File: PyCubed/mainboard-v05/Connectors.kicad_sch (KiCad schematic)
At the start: 28 parts, among them J1 503182-1852, J11 35362-0650, J13 USB_C_pycubed, J16 1985807, J18 1985807, J19 35362-0650, J2 Conn_01x05, J20 35362-0650, J21 35362-0650, J22 35362-0650, J23 35362-0650, J3 35362-0650, J4 35362-0650, J8 1985807, J9 1985807, U8 MR25H40MDF

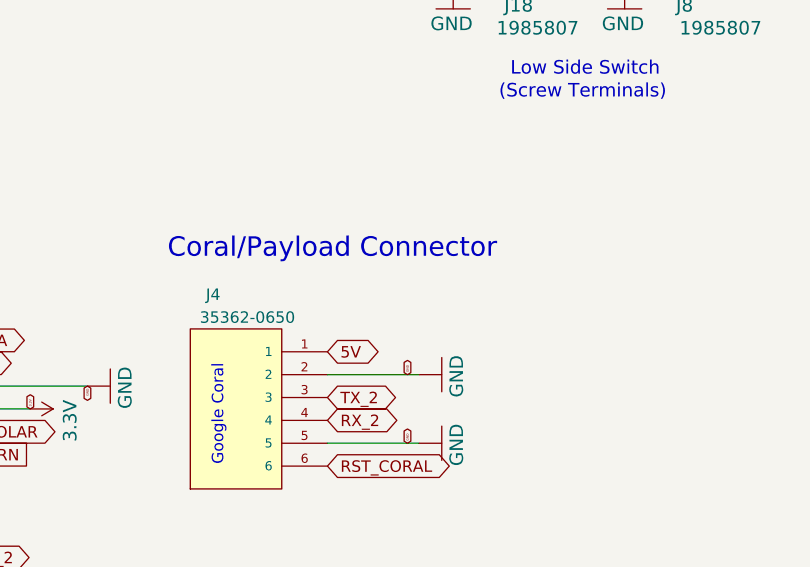
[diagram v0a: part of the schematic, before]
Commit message: final updates after JLC i2c error
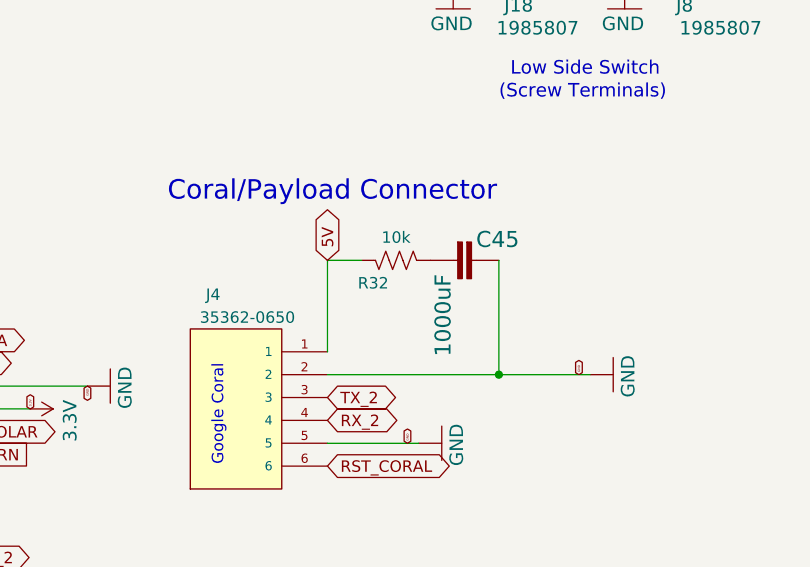
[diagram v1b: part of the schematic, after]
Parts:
- added C45: 1000uF, Capacitor_Tantalum_SMD:CP_EIA-7361-38_AVX-V, symbol mainboard:2.2UF-0603-10V-20%
- added R32: 10k, Resistor_SMD:R_0603_1608Metric, symbol Device:R_US
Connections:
- net 5V: now also R32.2
- net GND: now also C45.1
- new net: C45.2, R32.1
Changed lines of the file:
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@@
   (junction (at 123.19 78.74) (diameter 0) (color 0 0 0 0)
+  )
+  (junction (at 199.39 132.08) (diameter 0) (color 0 0 0 0)
   )
   (junction (at 242.57 41.91) (diameter 0) (color 0 0 0 0)
@@
     (stroke (width 0) (type default) (color 0 0 0 0))
   )
-  (wire (pts (xy 180.34 132.08) (xy 190.5 132.08))
+  (wire (pts (xy 199.39 132.08) (xy 209.55 132.08))
     (stroke (width 0) (type default) (color 0 0 0 0))
   )
@@
     (stroke (width 0) (type default) (color 0 0 0 0))
   )
+  (wire (pts (xy 199.39 119.38) (xy 199.39 132.08))
+    (stroke (width 0) (type default) (color 0 0 0 0))
+  )
   (wire (pts (xy 232.41 50.8) (xy 232.41 49.53))
     (stroke (width 0) (type default) (color 0 0 0 0))
@@
     (stroke (width 0) (type default) (color 0 0 0 0))
   )
+  (wire (pts (xy 180.34 119.38) (xy 184.15 119.38))
+    (stroke (width 0) (type default) (color 0 0 0 0))
+  )
   (wire (pts (xy 148.59 55.88) (xy 151.13 55.88))
     (stroke (width 0) (type default) (color 0 0 0 0))
@@
     (stroke (width 0) (type default) (color 0 0 0 0))
   )
+  (wire (pts (xy 180.34 132.08) (xy 199.39 132.08))
+    (stroke (width 0) (type default) (color 0 0 0 0))
+  )
   (wire (pts (xy 113.03 33.02) (xy 123.19 33.02))
     (stroke (width 0) (type default) (color 0 0 0 0))
@@
   )
   (wire (pts (xy 153.67 181.61) (xy 139.7 181.61))
+    (stroke (width 0) (type default) (color 0 0 0 0))
+  )
+  (wire (pts (xy 180.34 119.38) (xy 180.34 129.54))
     (stroke (width 0) (type default) (color 0 0 0 0))
   )
@@
     (effects (font (size 2.159 2.159)) (justify left bottom))
   )
-  (text "Coral/Payload Connector" (at 162.56 119.38 0)
+  (text "Coral/Payload Connector" (at 162.56 113.03 0)
     (effects (font (size 2.159 2.159)) (justify left bottom))
   )
@@
     )
   )
-  (global_label "5V" (shape bidirectional) (at 180.34 129.54 0) (fields_autoplaced)
-    (effects (font (size 1.27 1.27)) (justify left))
-    (property "Intersheet References" "${INTERSHEET_REFS}" (id 0) (at 0 0 0)
+  (global_label "5V" (shape bidirectional) (at 180.34 119.38 90) (fields_autoplaced)
+    (effects (font (size 1.27 1.27)) (justify left))
+    (property "Intersheet References" "${INTERSHEET_REFS}" (id 0) (at 50.8 299.72 0)
       (effects (font (size 1.27 1.27)) hide)
     )
@@
     )
   )
-  (global_label "GND" (shape bidirectional) (at 189.23 132.08 90) (fields_autoplaced)
+  (global_label "GND" (shape bidirectional) (at 208.28 132.08 90) (fields_autoplaced)
     (effects (font (size 0.254 0.254)) (justify left))
-    (property "Intersheet References" "${INTERSHEET_REFS}" (id 0) (at 0 0 0)
+    (property "Intersheet References" "${INTERSHEET_REFS}" (id 0) (at 19.05 0 0)
       (effects (font (size 1.27 1.27)) hide)
     )
@@
     (pin "1")
   )
-  (symbol (lib_id "mainboard:GND") (at 193.04 132.08 90) (unit 1)
-    (in_bom yes) (on_board yes)
-    (property "Reference" "#GND0122" (id 0) (at 193.04 132.08 0)
-      (effects (font (size 1.27 1.27)) hide)
-    )
-    (property "Value" "GND" (id 1) (at 195.58 134.62 0)
-      (effects (font (size 1.4986 1.4986)) (justify left bottom))
-    )
-    (property "Footprint" "" (id 2) (at 193.04 132.08 0)
-      (effects (font (size 1.27 1.27)) hide)
-    )
-    (property "Datasheet" "" (id 3) (at 193.04 132.08 0)
+  (symbol (lib_id "mainboard:GND") (at 212.09 132.08 90) (unit 1)
+    (in_bom yes) (on_board yes)
+    (property "Reference" "#GND0122" (id 0) (at 212.09 132.08 0)
+      (effects (font (size 1.27 1.27)) hide)
+    )
+    (property "Value" "GND" (id 1) (at 214.63 134.62 0)
+      (effects (font (size 1.4986 1.4986)) (justify left bottom))
+    )
+    (property "Footprint" "" (id 2) (at 212.09 132.08 0)
+      (effects (font (size 1.27 1.27)) hide)
+    )
+    (property "Datasheet" "" (id 3) (at 212.09 132.08 0)
       (effects (font (size 1.27 1.27)) hide)
     )
@@
       (effects (font (size 1.27 1.27)) hide)
     )
+    (pin "1")
+    (pin "2")
+  )
+  (symbol (lib_id "Device:R_US") (at 187.96 119.38 270) (mirror x) (unit 1)
+    (in_bom yes) (on_board yes)
+    (property "Reference" "R32" (id 0) (at 185.42 121.92 90))
+    (property "Value" "10k" (id 1) (at 187.96 116.84 90))
+    (property "Footprint" "Resistor_SMD:R_0603_1608Metric" (id 2) (at 187.706 118.364 90)
+      (effects (font (size 1.27 1.27)) hide)
+    )
+    (property "Datasheet" "" (id 3) (at 187.96 119.38 0)
+      (effects (font (size 1.27 1.27)) hide)
+    )
+    (property "Description" "10k 0603" (id 4) (at 187.96 121.92 0)
+      (effects (font (size 1.27 1.27)) hide)
+    )
+    (pin "1")
+    (pin "2")
+  )
+  (symbol (lib_id "mainboard:2.2UF-0603-10V-20%") (at 194.31 119.38 270) (unit 1)
+    (in_bom yes) (on_board yes)
+    (property "Reference" "C45" (id 0) (at 196.85 118.11 90)
+      (effects (font (size 1.778 1.778)) (justify left bottom))
+    )
+    (property "Value" "1000uF" (id 1) (at 192.151 120.904 0)
+      (effects (font (size 1.778 1.778)) (justify left bottom))
+    )
+    (property "Footprint" "Capacitor_Tantalum_SMD:CP_EIA-7361-38_AVX-V" (id 2) (at 194.31 119.38 0)
+      (effects (font (size 1.27 1.27)) hide)
+    )
+    (property "Datasheet" "" (id 3) (at 194.31 119.38 0)
+      (effects (font (size 1.27 1.27)) hide)
+    )
+    (property "Description" "0.1uF +-10% 50V X7R 0603" (id 4) (at 194.31 119.38 0)
+      (effects (font (size 1.27 1.27)) hide)
+    )
